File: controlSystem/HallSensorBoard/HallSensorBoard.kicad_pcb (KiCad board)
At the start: 2 copper layers, 12.7 x 16.8 mm, 5 parts, among them J1 22-23-2031, U1 DRV5056-Q1

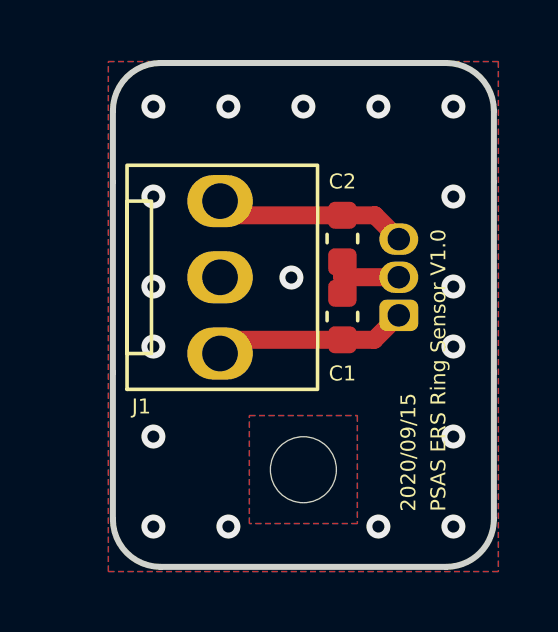
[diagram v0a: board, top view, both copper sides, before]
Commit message: Moved hall sensor board libraries to psas-kicad
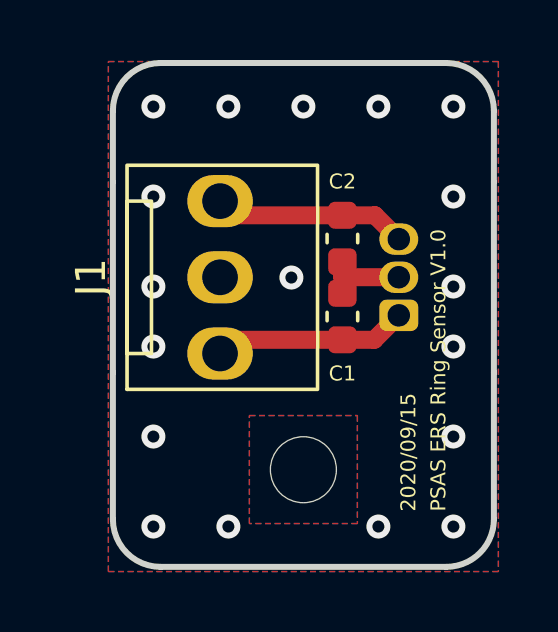
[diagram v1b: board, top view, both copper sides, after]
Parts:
- J1: footprint 22-23-2031:22-23-2031 -> psas-footprints:U-TI-22-23-2031
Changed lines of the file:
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@@
   )
   (net 0 "")
-  (net 1 "Net-(U1-Pad1)")
+  (net 1 "Net-(C1-Pad1)")
   (net 2 "GND")
-  (net 3 "Net-(J1-Pad3)")
+  (net 3 "Net-(C2-Pad1)")
   (footprint "Capacitor_SMD:C_0603_1608Metric" (layer "F.Cu")
     (at 156.3 101.5 90)
@@
     (fp_line (start 0.8 0.4) (end -0.8 0.4) (layer "F.Fab") (width 0.1))
     (pad "1" smd roundrect (at -0.775 0 90) (size 0.9 0.95) (layers "F.Cu" "F.Paste" "F.Mask") (roundrect_rratio 0.25)
-      (net 1 "Net-(U1-Pad1)") (pintype "passive"))
+      (net 1 "Net-(C1-Pad1)") (pintype "passive"))
     (pad "2" smd roundrect (at 0.775 0 90) (size 0.9 0.95) (layers "F.Cu" "F.Paste" "F.Mask") (roundrect_rratio 0.25)
       (net 2 "GND") (pintype "passive"))
@@
     (fp_line (start 0.8 -0.4) (end 0.8 0.4) (layer "F.Fab") (width 0.1))
     (pad "1" smd roundrect (at -0.775 0 270) (size 0.9 0.95) (layers "F.Cu" "F.Paste" "F.Mask") (roundrect_rratio 0.25)
-      (net 3 "Net-(J1-Pad3)") (pintype "passive"))
+      (net 3 "Net-(C2-Pad1)") (pintype "passive"))
     (pad "2" smd roundrect (at 0.775 0 270) (size 0.9 0.95) (layers "F.Cu" "F.Paste" "F.Mask") (roundrect_rratio 0.25)
       (net 2 "GND") (pintype "passive"))
@@
     )
   )
-  (footprint "22-23-2031:22-23-2031" (layer "F.Cu")
+  (footprint "psas-footprints:U-TI-22-23-2031" (layer "F.Cu")
     (at 152.221875 100.1923 90)
     (property "Sheetfile" "HallSensorBoard.kicad_sch")
     (property "Sheetname" "")
     (attr through_hole)
-    (fp_text reference "J1" (at -4.3077 -2.621875 unlocked) (layer "F.SilkS")
-      (effects (font (size 0.5 0.5) (thickness 0.12)))
+    (fp_text reference "J1" (at 0 -4.3 90 unlocked) (layer "F.SilkS")
+      (effects (font (size 1 1) (thickness 0.15)))
     )
     (fp_text value "22-23-2031" (at 0 -2.8 90 unlocked) (layer "F.Fab")
@@
       (effects (font (size 1 1) (thickness 0.15)))
     )
+    (fp_rect (start -3.735 -3.1) (end 3.735 3.25) (layer "F.SilkS") (width 0.12) (fill none))
     (fp_rect (start -2.54 -3.1) (end 2.54 -2.286) (layer "F.SilkS") (width 0.12) (fill none))
-    (fp_rect (start -3.735 -3.1) (end 3.735 3.25) (layer "F.SilkS") (width 0.12) (fill none))
     (pad "1" thru_hole oval (at -2.54 0 90) (size 1.74 2.19) (drill 1.19) (layers *.Cu *.Mask)
-      (net 1 "Net-(U1-Pad1)") (pinfunction "Pin_1") (pintype "passive"))
+      (net 1 "Net-(C1-Pad1)") (pinfunction "Pin_1") (pintype "passive"))
     (pad "2" thru_hole oval (at 0 0 90) (size 1.74 2.19) (drill 1.19) (layers *.Cu *.Mask)
       (net 2 "GND") (pinfunction "Pin_2") (pintype "passive"))
     (pad "3" thru_hole oval (at 2.54 0 90) (size 1.74 2.19) (drill 1.19) (layers *.Cu *.Mask)
-      (net 3 "Net-(J1-Pad3)") (pinfunction "Pin_3") (pintype "passive"))
-    (model "${KIPRJMOD}/022232031.stp"
+      (net 3 "Net-(C2-Pad1)") (pinfunction "Pin_3") (pintype "passive"))
+    (model "${PSAS_LIBRARIES}/psas-3dmodels/U-TI-022232031.stp"
       (offset (xyz 0 0 0))
       (scale (xyz 1 1 1))
@@
     (fp_line (start 2.51 -0.9775) (end 0.03 -0.9775) (layer "B.Fab") (width 0.1))
     (pad "1" thru_hole roundrect (at 0 0 90) (size 1.05 1.3) (drill 0.75) (layers *.Cu *.Mask) (roundrect_rratio 0.238)
-      (net 1 "Net-(U1-Pad1)") (pinfunction "VCC") (pintype "power_in"))
+      (net 1 "Net-(C1-Pad1)") (pinfunction "VCC") (pintype "power_in"))
     (pad "2" thru_hole oval (at 1.27 0 90) (size 1.05 1.3) (drill 0.75) (layers *.Cu *.Mask)
       (net 2 "GND") (pinfunction "GND") (pintype "power_in"))
     (pad "3" thru_hole oval (at 2.54 0 90) (size 1.05 1.3) (drill 0.75) (layers *.Cu *.Mask)
-      (net 3 "Net-(J1-Pad3)") (pinfunction "OUT") (pintype "output"))
+      (net 3 "Net-(C2-Pad1)") (pinfunction "OUT") (pintype "output"))
     (model "${KICAD6_3DMODEL_DIR}/Package_TO_SOT_THT.3dshapes/TO-92Flat.wrl"
       (offset (xyz 0 0 0))
@@
     )
   )
-  (zone (net 3) (net_name "Net-(J1-Pad3)") (layers F&B.Cu) (hatch edge 0.508)
+  (zone (net 3) (net_name "Net-(C2-Pad1)") (layers F&B.Cu) (hatch edge 0.508)
     (priority 2)
     (connect_pads (clearance 0.254))
